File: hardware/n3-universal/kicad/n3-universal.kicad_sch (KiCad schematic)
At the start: 127 parts, among them J1 Bornier_5.08, J10 JST-XH, J11 Bornier_5.08, J12 Bornier_5.08, J13 Support OLED, J14 Support I2C ext, J15 Header servo, J16 Header servo, J17 Header service, J18 Bornier_5.08, J19 Bornier_5.08, J2 Jack 5.5/2.1, J20 Header alim, J21 Support I2C libre, J22 Support I2C libre, J23 Bornier_5.08, J24 Bornier_5.08, J25 Bornier_5.08, J26 Bornier_5.08, J27 Bornier_5.08, J28 Support I2C libre, J29 JST-XH, J3 Bornier_5.08, J30 JST-XH, J31 Bornier_5.08, J32 Bornier_5.08, J33 Bornier_5.08, J34 Bornier_5.08, J35 Support module microSD, J36 Bornier_5.08, J37 Bornier_5.08, J4 Bornier_5.08, J5 Bornier_5.08, J6 Bornier_5.08, J7 JST-XH, J8 JST-XH, J9 JST-XH, K1 SRD-05VDC-SL-C, K2 SRD-05VDC-SL-C, K3 SRD-05VDC-SL-C, K4 SRD-05VDC-SL-C, K5 SRD-05VDC-SL-C, K6 SRD-05VDC-SL-C, Q1 BC337-40, Q10 BC337-40, Q11 NDP6020P, Q2 BC337-40, Q3 BC337-40, Q4 BC337-40, Q5 BC337-40, Q6 BC337-40, Q7 NDP6020P, Q8 BC337-40, Q9 BS250

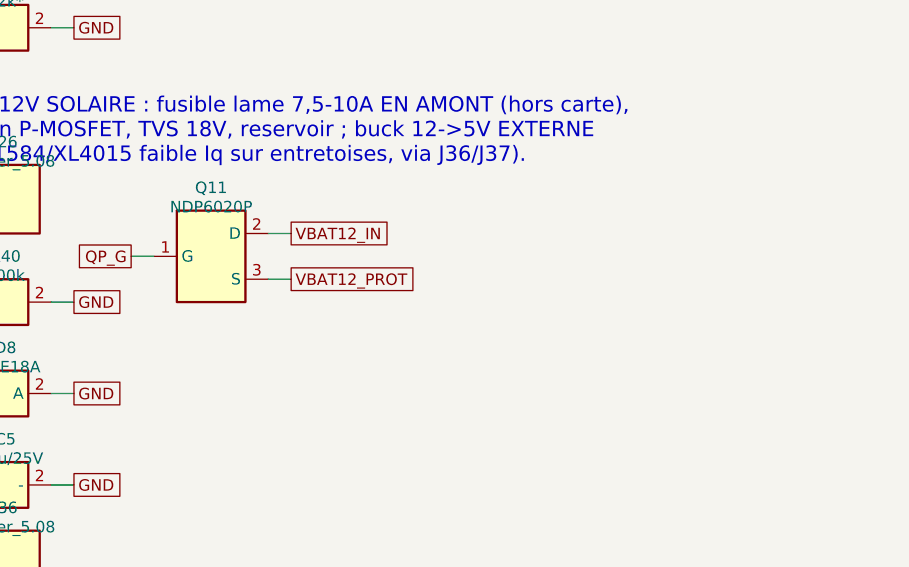
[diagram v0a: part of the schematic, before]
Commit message: [n3-universal] rev 0.1.2 : Q11 IRF4905 + zener D9, RV1 empreinte disque, trou nylon H5, serigraphie
- Q11 NDP6020P (VGS max +/-8 V) remplace par IRF4905PBF (VGS +/-20 V) : VGS = -VBAT en profil bus 12 V
- D9 1N4744A (15 V) grille-source de Q11, R40 limite son courant
- RV1 sur RV_Disc_D12mm_W5.4mm_P7.5mm (GEN-04), trou H5 vis nylon au coin secteur (GEN-05)
- serigraphie : JACK 5V, I2C J21/J22, polarites J18/J19/J25
- finalize_board : synchro empreintes/valeurs/descriptions + pistes D9
- table LCSC nettoyee des codes faux (C72503, C9135, C293822)
- DRC 0 erreur / 0 non connecte / 0 ecart de parite ; gerbers v0.1.2 (v0.1.1 retire)

Co-authored-by: Cursor <cursoragent@cursor.com>
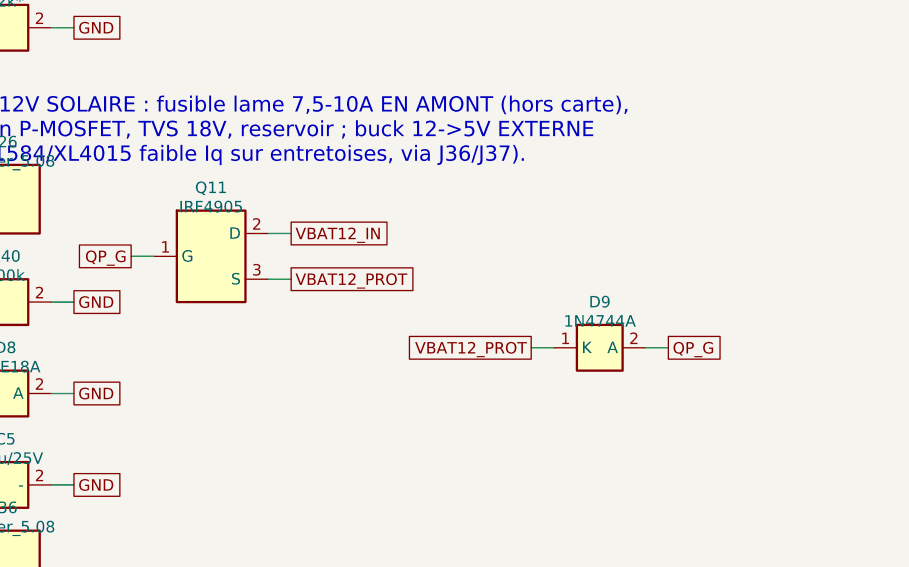
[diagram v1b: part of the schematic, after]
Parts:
- added D9: 1N4744A, n3u:D_DO-41_SOD81_P5.08mm_Vertical_AnodeUp, symbol n3u:D
- Q11: value NDP6020P -> IRF4905
- RV1: footprint n3u:CP_Radial_D10.0mm_P5.00mm -> n3u:RV_Disc_D12mm_W5.4mm_P7.5mm
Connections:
- net QP_G: now also D9.2 (A)
- net VBAT12_PROT: now also D9.1 (K)
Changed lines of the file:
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@@
     (title "n3-universal - carte porteuse UNIVERSELLE msp / n3pp / ffp5cs (bi-module WROOM / ESP32-S3)")
     (date "2026-10-06")
-    (rev "0.1.1")
+    (rev "0.1.2")
     (company "salle aeree n3")
     (comment 1 "Genere par hardware/n3-universal/generator/generate.py")
@@
     (property "Footprint" "n3u:BarrelJack_Horizontal" (at 60.96 45.72 0) (effects (font (size 1.27 1.27)) (hide yes)))
     (property "Datasheet" "~" (at 60.96 45.72 0) (effects (font (size 1.27 1.27)) (hide yes)))
-    (property "Description" "Entrée 5V 3A (jack, centre = +, ouverture bord gauche)" (at 60.96 45.72 0) (effects (font (size 1.27 1.27)) (hide yes)))
+    (property "Description" "Entrée 5V (jack DC-005 ~2,5 A, centre = +, ouverture bord gauche)" (at 60.96 45.72 0) (effects (font (size 1.27 1.27)) (hide yes)))
     (pin "1")
     (pin "3")
@@
     (exclude_from_sim no) (in_bom yes) (on_board yes) (dnp no)
     (property "Reference" "Q11" (at 393.70 124.46 0) (effects (font (size 1.27 1.27))))
-    (property "Value" "NDP6020P" (at 393.70 126.60 0) (effects (font (size 1.27 1.27))))
+    (property "Value" "IRF4905" (at 393.70 126.60 0) (effects (font (size 1.27 1.27))))
     (property "Footprint" "n3u:TO-220-3_Vertical" (at 393.70 132.08 0) (effects (font (size 1.27 1.27)) (hide yes)))
     (property "Datasheet" "~" (at 393.70 132.08 0) (effects (font (size 1.27 1.27)) (hide yes)))
-    (property "Description" "Anti-inversion P-MOSFET (1=G 2=D=entrée 3=S=sortie)" (at 393.70 132.08 0) (effects (font (size 1.27 1.27)) (hide yes)))
+    (property "Description" "Anti-inversion P-MOSFET 55V ±20V VGS (1=G 2=D=entrée 3=S=sortie)" (at 393.70 132.08 0) (effects (font (size 1.27 1.27)) (hide yes)))
     (pin "1")
     (pin "2")
@@
     (property "Footprint" "n3u:R_Axial_DIN0207_L6.3mm_D2.5mm_P10.16mm_Horizontal" (at 370.84 137.16 0) (effects (font (size 1.27 1.27)) (hide yes)))
     (property "Datasheet" "~" (at 370.84 137.16 0) (effects (font (size 1.27 1.27)) (hide yes)))
-    (property "Description" "Grille anti-inversion vers GND" (at 370.84 137.16 0) (effects (font (size 1.27 1.27)) (hide yes)))
+    (property "Description" "Grille anti-inversion vers GND (limite le courant de D9)" (at 370.84 137.16 0) (effects (font (size 1.27 1.27)) (hide yes)))
     (pin "1")
     (pin "2")
@@
     (property "Intersheetrefs" "${INTERSHEET_REFS}" (at 378.46 137.16 0)
       (effects (font (size 1.27 1.27)) (hide yes))))
+  (symbol (lib_id "n3u:D") (at 436.88 142.24 0) (unit 1)
+    (exclude_from_sim no) (in_bom yes) (on_board yes) (dnp no)
+    (property "Reference" "D9" (at 436.88 137.16 0) (effects (font (size 1.27 1.27))))
+    (property "Value" "1N4744A" (at 436.88 139.30 0) (effects (font (size 1.27 1.27))))
+    (property "Footprint" "n3u:D_DO-41_SOD81_P5.08mm_Vertical_AnodeUp" (at 436.88 142.24 0) (effects (font (size 1.27 1.27)) (hide yes)))
+    (property "Datasheet" "~" (at 436.88 142.24 0) (effects (font (size 1.27 1.27)) (hide yes)))
+    (property "Description" "Zener 15V grille-source de Q11 (K=source, A=grille) : VGS borné à -15 V" (at 436.88 142.24 0) (effects (font (size 1.27 1.27)) (hide yes)))
+    (pin "1")
+    (pin "2")
+    (instances (project "n3-universal" (path "/e48da96c-ccf9-5077-8ed8-2811f4041ce3" (reference "D9") (unit 1))))
+  )
+  (wire (pts (xy 431.80 142.24) (xy 429.26 142.24))
+    (stroke (width 0) (type default)))
+  (global_label "VBAT12_PROT" (shape passive) (at 429.26 142.24 180)
+    (effects (font (size 1.27 1.27)) (justify right))
+    (property "Intersheetrefs" "${INTERSHEET_REFS}" (at 429.26 142.24 0)
+      (effects (font (size 1.27 1.27)) (hide yes))))
+  (wire (pts (xy 441.96 142.24) (xy 444.50 142.24))
+    (stroke (width 0) (type default)))
+  (global_label "QP_G" (shape passive) (at 444.50 142.24 0)
+    (effects (font (size 1.27 1.27)) (justify left))
+    (property "Intersheetrefs" "${INTERSHEET_REFS}" (at 444.50 142.24 0)
+      (effects (font (size 1.27 1.27)) (hide yes))))
   (symbol (lib_id "n3u:D") (at 370.84 147.32 0) (unit 1)
     (exclude_from_sim no) (in_bom yes) (on_board yes) (dnp no)
@@
     (property "Reference" "RV1" (at 393.70 203.20 0) (effects (font (size 1.27 1.27))))
     (property "Value" "10D471K" (at 393.70 205.34 0) (effects (font (size 1.27 1.27))))
-    (property "Footprint" "n3u:CP_Radial_D10.0mm_P5.00mm" (at 393.70 208.28 0) (effects (font (size 1.27 1.27)) (hide yes)))
+    (property "Footprint" "n3u:RV_Disc_D12mm_W5.4mm_P7.5mm" (at 393.70 208.28 0) (effects (font (size 1.27 1.27)) (hide yes)))
     (property "Datasheet" "~" (at 393.70 208.28 0) (effects (font (size 1.27 1.27)) (hide yes)))
-    (property "Description" "Varistance 300VAC transitoires secteur — pattes à replier (pas réel 7,5 mm sur une empreinte 5,0 mm) : pose main, à exclure d'un assemblage machine ; le repère + de l'empreinte est sans objet" (at 393.70 208.28 0) (effects (font (size 1.27 1.27)) (hide yes)))
+    (property "Description" "Varistance 300VAC transitoires secteur (disque 10 mm, pas 7,5 mm)" (at 393.70 208.28 0) (effects (font (size 1.27 1.27)) (hide yes)))
     (pin "1")
     (pin "2")

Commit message: [n3-universal] rev 0.2 (WIP) : régénération complète — alim, cavaliers, borniers à vis, gardes
Point d'étape avant la fin du routage (freerouting en cours, 5 liaisons à
reprendre à la main) ; le PCB committé ici est intermédiaire.

generate.py 0.2 : rail capteurs Q7 IRF4905 + U1 LD1117V33 (JP1 bypass),
pont VBAT permanent (R38 + JP12 22k/100k, R49/C13, clamp D11 sur empreinte
double DO-35/SOD-123), Q12 IRF4905 anti-inversion + D12 1.5KE6.8A sur l'entrée
5 V, D8 1.5KE18A, cavaliers de forçage JP5-JP10 (K3 sans ON) + R61-R66, header
J38 CMD SENSE, borniers à vis 5,08 partout (bornier-4 HC-SR04), JP11 SD MISO,
diviseurs ADC/US par cavaliers JP13-JP21, TO-92 pas 2,54, TP1-4, 7 trous M3,
fusible sur empreinte universelle (clips 22,5 ou BLX-A 22,0), règle DRU
mains_creepage 6,4 mm, empilage 2 oz HAL sans plomb, SOURCING (Maroc / colis
LCSC, codes vérifiés le 2026-10-06), garde de recouvrement des étiquettes du
schéma, champ Description sur les empreintes (parité KiCad 10).

route_universal.py : API KiCad 10, retrait des pads A' avant chargement,
ponts A/A' du DevKit, keepouts COM resserrés, fentes COM allongées y66-83.
tidy_silkscreen.py : interdit d'entrer dans le courtyard d'un autre composant.
tools : check_silk_refs.py (nouveau, en CI), check_pcb_clearance.py
(bornier-4, couloirs USB avec offset), check_pinmap_vs_firmware.py (topologies
0.2). export_pcba.py : BOM/CPL PCBA dérivés de BOM.csv + CPL.
finalize_board.py : obsolète (garde-fou à l'exécution).

Docs : README (tableau 0.1.2 → 0.2, cavaliers), COMMANDE.md (JLCPCB, colis
d'import, achats Maroc), EVOLUTIONS_PROPOSEES (décisions actées), audit §14
(squelette), COMPOSANTS_FFP5CS.csv, hardware/README, COMMANDE_JLCPCB,
VERIFICATION, TUTO_PCB §4.bis.

Sources : empreintes dérivées de kicad-footprints (CC-BY-SA 4.0,
https://gitlab.com/kicad/libraries/kicad-footprints) ; freerouting 2.1.0
(https://github.com/freerouting/freerouting, GPL-3.0, outil non embarqué) ;
fiches ST LD1117, Infineon IRF4905, Littelfuse 1.5KE, Xuc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
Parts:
- removed Q10: BC337-40, n3u:TO-92_Inline, symbol n3u:NPN
- removed Q9: BS250, n3u:TO-92_Inline, symbol n3u:PMOS_DGS
- removed R36, R37: 100k, n3u:R_Axial_DIN0207_L6.3mm_D2.5mm_P10.16mm_Horizontal, symbol n3u:R
- added C10, C13, C6, C7, C8, C9: 100n, n3u:C_Disc_D5.0mm_W2.5mm_P5.00mm, symbol n3u:C
- added C11: 10u/25V, n3u:CP_Radial_D5.0mm_P2.50mm, symbol n3u:CP
- added C12: 100u/16V, n3u:CP_Radial_D6.3mm_P2.50mm, symbol n3u:CP
- added D11: BAT85, n3u:D_DO-35_SOD-123_Dual_P7.62mm, symbol n3u:D
- added D12: 1.5KE6.8A, n3u:D_DO-201AD_P15.24mm_Horizontal, symbol n3u:D
- added J38: Header CMD SENSE, n3u:PinHeader_1x08_P2.54mm_Vertical, symbol n3u:CONN_08
- added JP10, JP5, JP6, JP7, JP8, JP9: Jumper ON/OFF, n3u:PinHeader_1x03_P2.54mm_Vertical, symbol n3u:CONN_03
- added JP11: Jumper SD MISO, n3u:PinHeader_1x03_P2.54mm_Vertical, symbol n3u:CONN_03
- added JP12: Jumper profil, n3u:PinHeader_1x03_P2.54mm_Vertical, symbol n3u:CONN_03
- added JP13, JP14, JP15, JP16, JP17, JP18, JP19, JP20, JP21: Jumper profil, n3u:PinHeader_1x02_P2.54mm_Vertical, symbol n3u:CONN_02
- added Q12: IRF4905, n3u:TO-220-3_Vertical_GDS, symbol n3u:PMOS_GDS
- added R48: 10k, n3u:R_Axial_DIN0207_L6.3mm_D2.5mm_P10.16mm_Horizontal, symbol n3u:R
- added R49, R50, R51, R52, R53, R54, R61, R62, R64, R65, R66: 1k, n3u:R_Axial_DIN0207_L6.3mm_D2.5mm_P10.16mm_Horizontal, symbol n3u:R
- added R57, R58: 100k, n3u:R_Axial_DIN0207_L6.3mm_D2.5mm_P10.16mm_Horizontal, symbol n3u:R
- added TP1: GND, n3u:TestPoint_THTPad_D2.0mm_Drill1.0mm, symbol n3u:TP
- added TP2: +5V, n3u:TestPoint_THTPad_D2.0mm_Drill1.0mm, symbol n3u:TP
- added TP3: +3V3_SW, n3u:TestPoint_THTPad_D2.0mm_Drill1.0mm, symbol n3u:TP
- added TP4: +3V3, n3u:TestPoint_THTPad_D2.0mm_Drill1.0mm, symbol n3u:TP
- added U1: LD1117V33, n3u:TO-220-3_Vertical_LDO, symbol n3u:LDO
- D8: value P6KE18A -> 1.5KE18A
- F1: footprint n3u:Fuse_5x20_Horizontal -> n3u:Fuse_5x20_Universal
- J10, J29, J30: value JST-XH -> Bornier_5.08; footprint n3u:JST_XH_B3B-XH-A_1x03_P2.50mm_Vertical -> n3u:TerminalBlock_bornier-3_P5.08mm
- J7, J8, J9: value JST-XH -> Bornier_5.08; footprint n3u:JST_XH_B4B-XH-A_1x04_P2.50mm_Vertical -> n3u:TerminalBlock_bornier-4_P5.08mm
- Q1, Q2, Q3, Q4, Q5, Q6, Q8: footprint n3u:TO-92_Inline -> n3u:TO-92_Inline_Wide_CBE
- Q11: footprint n3u:TO-220-3_Vertical -> n3u:TO-220-3_Vertical_GDS
- Q7: value NDP6020P -> IRF4905; footprint n3u:TO-220-3_Vertical -> n3u:TO-220-3_Vertical_GDS
- R17, R18, R19: value 2k* -> 2k
- R27, R43, R44, R45, R46, R47: value 10k* -> 10k
- R38: value 100k* -> 100k
- R39: value 22k* -> 22k
- RV1: value 10D471K -> 14D471K; footprint n3u:RV_Disc_D12mm_W5.4mm_P7.5mm -> n3u:RV_Disc_D15.5mm_W8mm_P7.5mm
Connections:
- net VBAT_SW is gone; now on net VBAT_SENSE: R38.1
- net +3V3: now also D11.1 (K), R61.1, R62.1, R64.1, R65.1, R66.1, TP4.1; no longer JP1.1, Q7.3 (S), R35.1
- net +3V3_SW: now also C12.1 (+), TP3.1, U1.2 (OUT); no longer JP1.2, Q7.2 (D)
- net +5V: now also JP1.1, Q7.2 (D), R35.1, D12.1 (K), J38.8, Q12.3 (S), TP2.1; no longer J1.1, J2.1 (TIP), J37.1
- net ADC_A: now also C6.1, R50.2; no longer J31.2, R43.1
- net ADC_B: now also C7.1, R51.2; no longer J32.2, R44.1
- net ADC_C: now also C8.1, R52.2; no longer J33.2, R45.1
- net ADC_D: now also C9.1, R53.2; no longer J34.2, R46.1
- net ADC_E: now also C10.1, R54.2; no longer J12.2, R27.1
- net ADC_VBAT: now also C13.1, D11.2 (A), R49.2; no longer R38.2, R39.1
- net GATE_B: now also R48.1
- net GND: now also C10.2, C11.2 (-), C12.2 (-), C13.2, C6.2, C7.2, C8.2, C9.2, D12.2 (A), J38.7, JP10.3, JP13.2, JP14.2, JP15.2, JP16.2, JP17.2, JP18.2, JP19.2, JP20.2, JP5.3, JP6.3, JP7.3, JP8.3, JP9.3, R48.2, R57.2, R58.2, TP1.1, U1.1 (GND); no longer R17.2, R18.2, R19.2, R27.2, R43.2, R44.2, R45.2, R46.2
- net REL1_B: now also JP5.2
- net REL1_SW: now also J38.1
- net REL2_B: now also JP6.2
- net REL2_SW: now also J38.2
- net REL3_B: now also JP7.2
- net REL3_SW: now also J38.3
- net REL4_B: now also JP8.2
- net REL4_SW: now also J38.4
- net REL5_B: now also JP9.2
- net REL5_SW: now also J38.5
- net REL6_B: now also JP10.2
- net REL6_SW: now also J38.6
- net SD_MISO: now also JP11.2; no longer A1.19 (GPIO12), A2.20 (GPIO14)
- net US2: now also JP21.2; no longer R47.2
- new net ADC_A_DIV: JP16.1, R43.2
- new net ADC_A_IN: J31.2, R43.1, R50.1
- new net ADC_B_DIV: JP17.1, R44.2
- new net ADC_B_IN: J32.2, R44.1, R51.1
- new net ADC_C_DIV: JP18.1, R45.2
- new net ADC_C_IN: J33.2, R45.1, R52.1
- new net ADC_D_DIV: JP19.1, R46.2
- new net ADC_D_IN: J34.2, R46.1, R53.1
- new net ADC_E_DIV: JP20.1, R27.2
- new net ADC_E_IN: J12.2, R27.1, R54.1
- new net DHT_EXT_PU: JP21.1, R47.2
- new net LDO_IN: C11.1 (+), JP1.2, Q7.3 (S), U1.3 (IN)
- new net Q12_G: Q12.1 (G), R57.1
- new net REL1_ON: JP5.1, R61.2
- new net REL2_ON: JP6.1, R62.2
- new net REL4_ON: JP8.1, R64.2
- new net REL5_ON: JP9.1, R65.2
- new net REL6_ON: JP10.1, R66.2
- new net SD_MISO_S3: A2.20 (GPIO14), JP11.1
- new net SD_MISO_W: A1.19 (GPIO12), JP11.3
- new net US_AQUA_DIV: JP13.1, R17.2
- new net US_POTA_DIV: JP15.1, R19.2
- new net US_TANK_DIV: JP14.1, R18.2
- new net VBAT_100K: JP12.3, R58.1
- new net VBAT_22K: JP12.1, R39.1
- new net VBAT_DIV: JP12.2, R38.2, R49.1
- new net VIN_RAW: J1.1, J2.1 (TIP), J37.1, Q12.2 (D)
- no-connect marks 8 -> 9
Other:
- note added: "3x HC-SR04 (5V) sur borniers 5,08, mode mono-broche TRIG=ECHO (sensor_ultrasonic.cpp). Echo 5V ramené à 3V3 par pont 1k/2k ; le 2k est en circuit si JP13/14/15 FERMÉ (profil ffp5cs). OUVERT sur msp (PLUIE sur US1, DHT ext sur US2) et pour l'option wroom-sd (JP15)."
- note added: "6 RELAIS K1..K6 — commande ACTIVE HAUT (base 1k + pull-down 10k : etat sur au boot). WROOM : GPIO16/17/18/19/23/25 — S3 : IO15/16/17/18/48/45. Le role de chaque canal depend du firmware (voir les sections PINMAP_UNIVERSAL). Borniers : 1=NC 2=COM 3=NO. FORCAGE JP5..JP10 (1x3 sur la base) : SANS cavalier = AUTO (firmware) ; 1-2 = ON force (+3V3 via 1k) ; 2-3 = OFF force (base a GND). K3 (chauffage)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"
- note added: "ALIMENTATION 5V (3A recommandé) — jack OU bornier J1 OU sortie buck J37, tous sur VIN_RAW. Q12 (IRF4905, VGS=-5V) = anti-inversion : un fil inversé ne détruit plus la carte. D12 = TVS 6,8V. D5 protège le rail si l'USB du DevKit est branché en même temps."
- note added: "Distribution 5V / 3V3-capteurs / GND : borniers a vis + rail header. Points de test TP1..TP4."
- note added: "ENTREES ANALOGIQUES PARTAGEES ADC_A..D : LDR msp (JP16-19 FERMES) ou sondes sol n3pp (JP OUVERTS). ADC_E = HumidSol msp / Luminosite n3pp / LDR ffp5cs (JP20). Pluie msp = net US1 ; DHT ext msp = net US2 (pull-up R47 si JP21 FERME) — roles disjoints."
- note added: "I2C : OLED SSD1306 0x3C + 3 supports extension (DS3231, INA226...)."
- note added: "J38 CMD SENSE : collecteurs des 6 transistors relais (0V = relais colle, 5V = repos) + GND + 5V — retour d'etat reel pour un expandeur deporte (PCF8574 via diviseur)."
- note added: "LUMIERE : LDR déportée sur J12, net ADC_E (GPIO36 WROOM / IO6 S3). Bas de pont R27 10k en circuit si JP20 FERMÉ (LDR n3pp/ffp5cs) ; OUVERT pour un module AO (msp HumiditeSol). Filtre série 1k + 100n sur chaque entrée ADC (fils longs)."
- note added: "PONT DIVISEUR VBAT PERMANENT (rev 0.2, plus de coupure BS250) : R38 100k + JP12 : 1-2 = 22k (bus 12V, ffp5cs) ; 2-3 = 100k (1S Li-ion, msp/n3pp). R49/C13 filtre, D11 clamp 3V3."
- note added: "POWER-GATE +3V3_SW (GPIO13) — rev 0.2 : LDO DEDIE U1 (LD1117V33) alimente par le 5V commute par Q7 (IRF4905, VGS=-5V). R35 : rail OFF par defaut ; R48 : pull-down base Q8. JP1 FERME par defaut (rail permanent, ffp5cs) ; OTER JP1 sur les profils batterie -> tout le rail capteurs (LDO compris) est coupe en veille."
- note added: "PROFIL BUS 12V SOLAIRE : fusible lame 7,5-10A EN AMONT (hors carte), anti-inversion P-MOSFET Q11, TVS 18V D8 (1.5KE18A, DO-201), reservoir ; buck 12->5V EXTERNE (module MP1584/XL4015 faible Iq sur entretoises, via J36/J37 ; J37 passe par Q12)."
- note added: "PROFIL SECTEUR : Hi-Link HLK-20M05 EMBARQUE (5V/3,6A) + fusible T1A (porte-fusible a capot, empreinte universelle pas 22,5-22,6) + varistance 10 ou 14 mm. Le corps du module enjambe la frontiere secteur/logique (fente fraisee dessous). ZONE 230V = DANGER."
- note added: "SITE A1 : ESP32 DevKit V1 (30 broches, socketé) — UN SEUL module peuplé (A1 OU A2). Empreinte à DEUX entraxes (25,4 = rangée A, 27,94 = rangée A') : souder le support droit là où tombent les broches du module. Envs carte universelle : msp/n3pp esp32dev_universal_test, ffp5cs wroom-universal-test. Sur une unité ffp5cs, ÔTER JP1 avant un flash UART (le pull-up R24 sur GPIO2 bloque le bootloader)."
- note added: "SITE A2 : ESP32-S3-DevKitC-1 44 broches, couche, USB vers le bord droit. UN SEUL module peuple (A1 OU A2). Cartographies PINMAP_UNIVERSAL des 3 firmwares."
- note added: "microSD : module SPI 3V3 sockete. JP2/3/4/11 : source des lignes CS/SCK/MOSI/MISO = S3 natif (1-2, defaut) ou WROOM env wroom-sd (2-3). MISO WROOM = GPIO12/MTDI : efuse VDD_SDIO=3V3 OBLIGATOIRE avant (strap tension flash)."
- note removed: "3x HC-SR04 (5V), mode mono-broche TRIG=ECHO (sensor_ultrasonic.cpp). Echo 5V ramené à 3V3 par pont 1k/2k sur chaque canal."
- note removed: "6 RELAIS K1..K6 — commande ACTIVE HAUT (base 1k + pull-down 10k : etat sur au boot). WROOM : GPIO16/17/18/19/23/25 — S3 : IO15/16/17/18/48/45. Le role de chaque canal depend du firmware (voir les sections PINMAP_UNIVERSAL). Borniers : 1=NC 2=COM 3=NO. SRD Form C = 7A/240VAC et 3A inductif REELS par contact (le 10A ne vaut qu'en 125VAC ou en Form A). ZONE SECTEUR ISOLEE sur le PCB (fentes + 3mm mi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"
- note removed: "ALIMENTATION 5V (3A recommandé) — jack OU bornier. D5 protège le rail si l'USB du DevKit est branché en même temps."
- note removed: "Distribution 5V / 3V3-capteurs / GND : borniers a vis + rail header."
- note removed: "ENTREES ANALOGIQUES PARTAGEES ADC_A..D : LDR msp (poser R43-46) ou sondes sol n3pp (sans R). ADC_E = HumidSol msp / Luminosite n3pp / LDR ffp5cs. Pluie msp = net US1 ; DHT ext msp = net US2 (roles disjoints)."
- note removed: "I2C : OLED SSD1306 0x3C + header extension (DS3231 si besoin)."
- note removed: "LUMIERE : LDR déportée sur J12, net ADC_E (GPIO36 WROOM / IO6 S3). Bas de pont R27 10k : A POSER pour une LDR, ABSENT pour un module à sortie AO."
- note removed: "PONT DIVISEUR VBAT COMMUTE : actif seulement quand +3V3_SW est present. R38/R39 SELON PROFIL : 1S Li-ion = 100k/100k ; bus 12V = 100k/22k."
- note removed: "POWER-GATE +3V3_SW (GPIO13, topologie n3pp-msp rev 0.2) : JP1 FERME par defaut (rail permanent, ffp5cs) ; OTER JP1 sur les profils batterie -> tout le rail capteurs est coupe en veille."
- note removed: "PROFIL BUS 12V SOLAIRE : fusible lame 7,5-10A EN AMONT (hors carte), anti-inversion P-MOSFET, TVS 18V, reservoir ; buck 12->5V EXTERNE (module MP1584/XL4015 faible Iq sur entretoises, via J36/J37)."
- note removed: "PROFIL SECTEUR : Hi-Link HLK-20M05 EMBARQUE (5V/3,6A) + fusible T1A + varistance 300VAC. Le corps du module enjambe la frontiere secteur/logique (fente fraisee dessous). ZONE 230V = DANGER."
- note removed: "SITE A1 : ESP32 DevKit V1 (30 broches, socketé) — UN SEUL module peuplé (A1 OU A2). Envs carte universelle : msp/n3pp esp32dev_universal_test, ffp5cs wroom-universal-test. Sur une unité ffp5cs, ÔTER JP1 avant un flash UART (le pull-up R24 sur GPIO2 bloque le bootloader)."
- note removed: "SITE A2 : ESP32-S3-DevKitC-1 44 broches. UN SEUL module peuple (A1 OU A2). Cartographies PINMAP_UNIVERSAL des 3 firmwares."
- note removed: "microSD : module SPI 3V3 sockete. JP2/3/4 : source des lignes CS/SCK/MOSI = S3 natif (1-2, defaut) ou WROOM env wroom-sd (2-3). MISO = net partage direct (A1-GPIO12 / A2-IO14)."
- moved on the sheet: C5, D8, D9, J25, J26, J36, J37, J7, J8, J9, JP1, Q11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

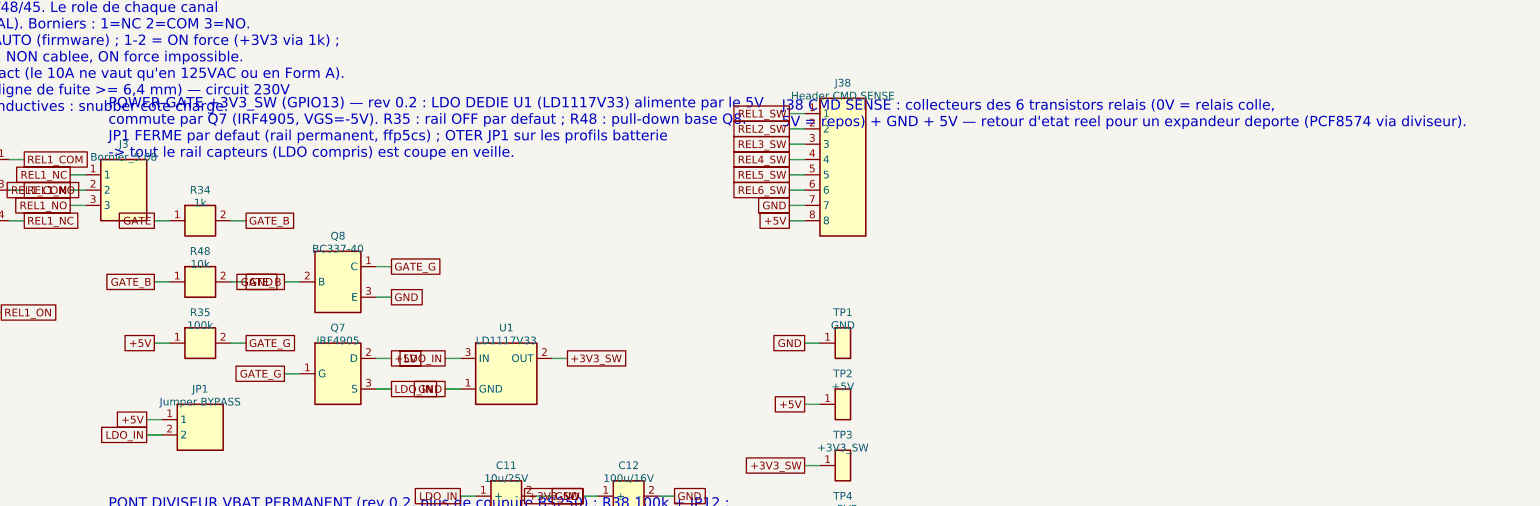
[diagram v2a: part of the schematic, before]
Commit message: hardware/n3-universal rev 0.2.1 : Q7 inversé (rail capteurs jamais coupé), simulation SPICE, garde d'orientation MOSFET
Simulation ngspice des blocs analogiques de la carte universelle (simulation/SIMULATION.md) :
Q7 (IRF4905, commutation du 5 V vers le LDO capteurs) était câblé drain=+5V / source=LDO_IN,
comme les anti-inversion Q11/Q12. Pour un canal P la diode interne va de D vers S : JP1 ôté
et GPIO13 bas, LDO_IN restait à 4,6 V et +3V3_SW à 3,3 V. Le rail capteurs ne se coupait
jamais sur les profils msp/n3pp. ERC/DRC ne voient pas ce défaut (netlist correcte, circuit faux).

- generator/generate.py : Q7 source=+5V, drain=LDO_IN ; REV 0.2.1 ; champs Sim.* par composant
  (sim_fields) et kicad/n3u_sim.lib généré depuis simulation/models.lib (translittéré ASCII :
  le lecteur SPICE de KiCad s'arrête sur un caractère non ASCII, même en commentaire).
- kicad/n3-universal.kicad_sch, BOM.csv : régénérés (seul changement électrique : broches 2/3 de Q7).
  ERC KiCad 8.0.9 : 0 erreur ; export netlist SPICE OK.
- kicad/n3-universal.kicad_pcb : retouche locale autour de Q7 (pads 2->LDO_IN, 3->+5V ; pistes +5V,
  LDO_IN, ADC_E), Description Q7, texte v0.2.1 au dos. Contrôle géométrique indépendant : 0 écart
  < 0,2 mm. Zones à remplir + DRC/parité KiCad 10 à relancer avant gerbers (README §0.2.1).
- tools/check_fet_orientation.py : garde CI — (rôle, net amont) par P-MOSFET, vérifiée dans le
  générateur et dans le .kicad_sch ; échoue sur le schéma 0.2.
- simulation/ : models.lib, harnais ngspice (spicelib.py), sim1 étage relais (Monte-Carlo),
  sim2 rail capteurs, sim3 entrées d'alim (Q12, chaîne 5 V -> DevKit, Q11/D8/D9), sim4 ponts
  de mesure + dynamique du rail 5 V, bench_kicad_netlist.py sur la netlist exportée par KiCad,
  tracés et résultats dans out/.
- README (hardware/, n3-universal/) : encadré « ne pas commander la 0.2 », section 0.2.1,
  marges relevées (budget 5 V vers le DevKit, appel servo 2,5 A, pont VBAT) documentées sans modification.

Co-Authored-By: Cla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
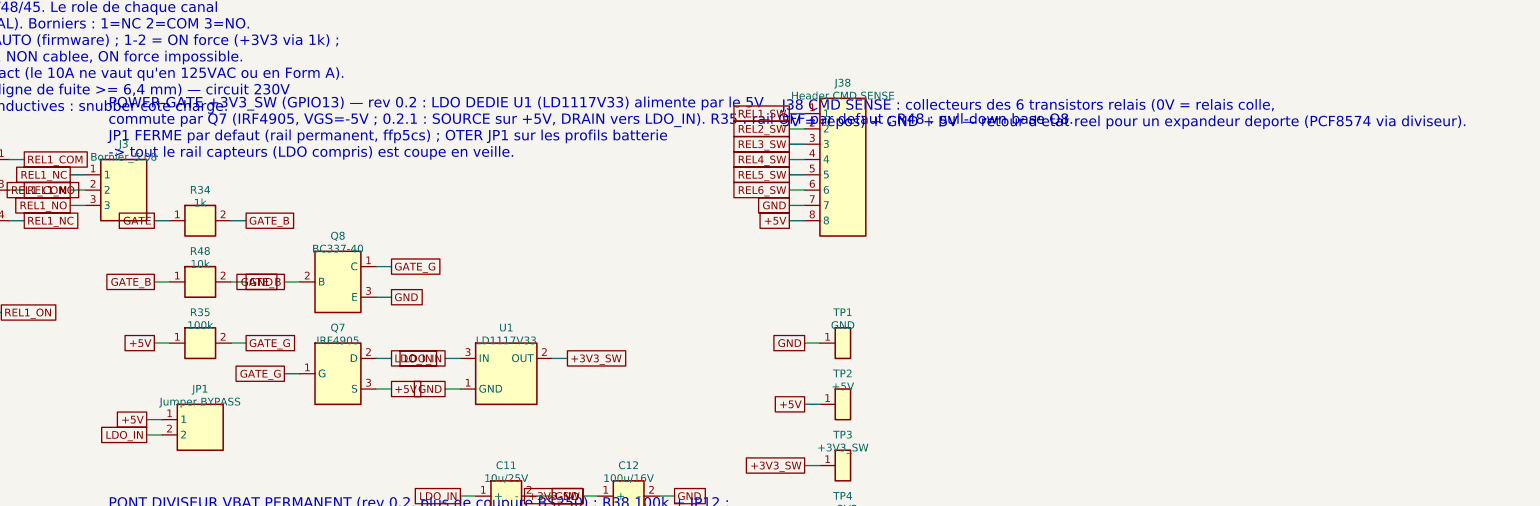
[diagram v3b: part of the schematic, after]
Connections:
- net +5V: now also Q7.3 (S); no longer Q7.2 (D)
- net LDO_IN: now also Q7.2 (D); no longer Q7.3 (S)
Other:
- note added: "POWER-GATE +3V3_SW (GPIO13) — rev 0.2 : LDO DEDIE U1 (LD1117V33) alimente par le 5V commute par Q7 (IRF4905, VGS=-5V ; 0.2.1 : SOURCE sur +5V, DRAIN vers LDO_IN). R35 : rail OFF par defaut ; R48 : pull-down base Q8. JP1 FERME par defaut (rail permanent, ffp5cs) ; OTER JP1 sur les profils batterie -> tout le rail capteurs (LDO compris) est coupe en veille."
- note removed: "POWER-GATE +3V3_SW (GPIO13) — rev 0.2 : LDO DEDIE U1 (LD1117V33) alimente par le 5V commute par Q7 (IRF4905, VGS=-5V). R35 : rail OFF par defaut ; R48 : pull-down base Q8. JP1 FERME par defaut (rail permanent, ffp5cs) ; OTER JP1 sur les profils batterie -> tout le rail capteurs (LDO compris) est coupe en veille."
